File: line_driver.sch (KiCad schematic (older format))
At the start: 30 parts, among them J7 DRV632

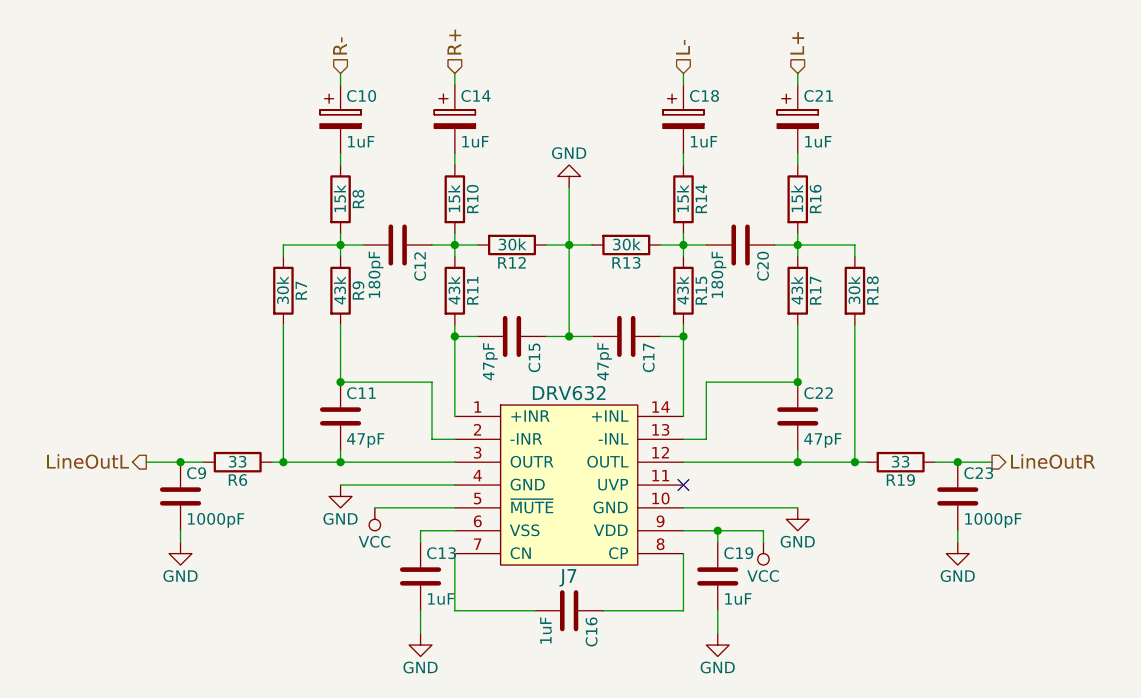
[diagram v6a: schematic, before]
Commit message: Voltage regulator adjustments and tidying
Switch to LD1117 component and add decoupling caps.
Add a decoupling cap to the audio switch
Shift some status LEDs to modules layer
Use ProMini instead of ProMicro
Update BOM
Update netlist
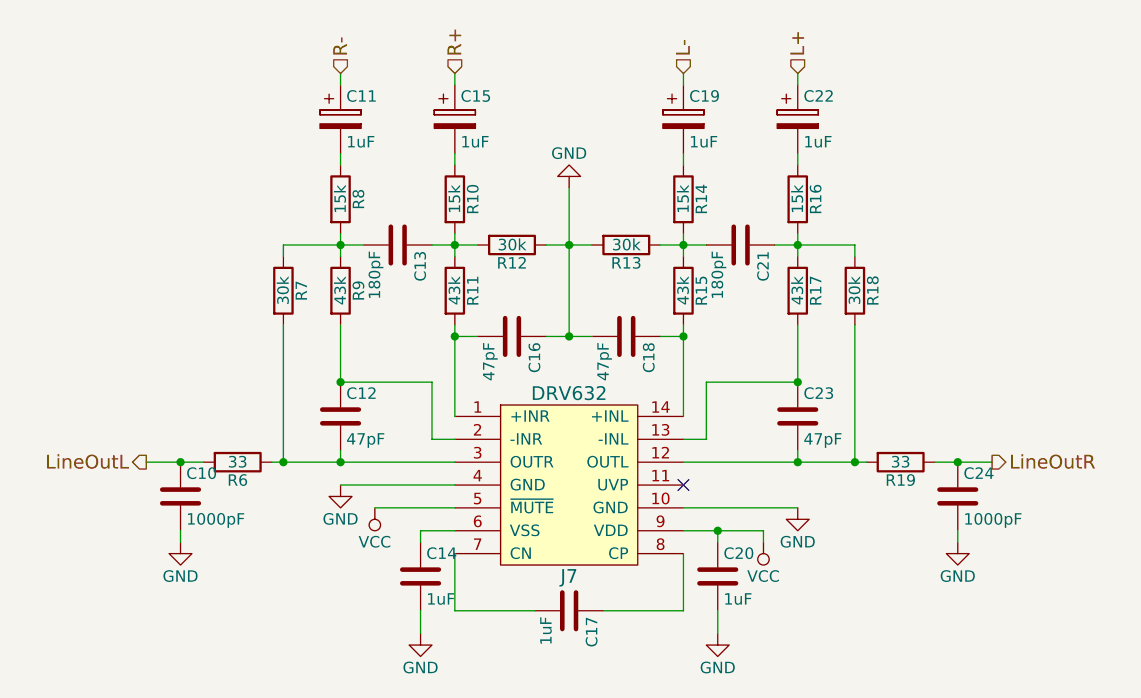
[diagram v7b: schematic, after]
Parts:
- C10: renamed from C9; footprint (none) -> blubaru:C_Disc_D5.5mm_W2.5mm_P2.50mm
- C11: renamed from C10; footprint (none) -> Capacitors_THT:CP_Radial_D4.0mm_P1.50mm
- C12: renamed from C11; footprint (none) -> blubaru:C_Disc_D5.5mm_W2.5mm_P2.50mm
- C13: renamed from C12; footprint (none) -> blubaru:C_Disc_D5.5mm_W2.5mm_P2.50mm
- C14: renamed from C13; footprint (none) -> blubaru:C_Disc_D5.5mm_W2.5mm_P2.50mm
- C15: renamed from C14; footprint (none) -> Capacitors_THT:CP_Radial_D4.0mm_P1.50mm
- C16: renamed from C15; footprint (none) -> blubaru:C_Disc_D5.5mm_W2.5mm_P2.50mm
- C17: renamed from C16; footprint (none) -> blubaru:C_Disc_D5.5mm_W2.5mm_P2.50mm
- C18: renamed from C17; footprint (none) -> blubaru:C_Disc_D5.5mm_W2.5mm_P2.50mm
- C19: renamed from C18; footprint (none) -> Capacitors_THT:CP_Radial_D4.0mm_P1.50mm
- C20: renamed from C19; footprint (none) -> blubaru:C_Disc_D5.5mm_W2.5mm_P2.50mm
- C21: renamed from C20; footprint (none) -> blubaru:C_Disc_D5.5mm_W2.5mm_P2.50mm
- C22: renamed from C21; footprint (none) -> Capacitors_THT:CP_Radial_D4.0mm_P1.50mm
- C23: renamed from C22; footprint (none) -> blubaru:C_Disc_D5.5mm_W2.5mm_P2.50mm
- C24: renamed from C23; footprint (none) -> blubaru:C_Disc_D5.5mm_W2.5mm_P2.50mm
- R19, R6: footprint (none) -> Resistors_THT:R_Axial_DIN0204_L3.6mm_D1.6mm_P1.90mm_Vertical
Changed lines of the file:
@@
 $EndComp
 $Comp
-L C C16
+L C C17
 U 1 1 59178EA2
 P 5800 3950
-F 0 "C16" H 5825 4050 50  0000 L CNN
+F 0 "C17" H 5825 4050 50  0000 L CNN
 F 1 "1uF" H 5825 3850 50  0000 L CNN
-F 2 "" H 5838 3800 50  0001 C CNN
+F 2 "blubaru:C_Disc_D5.5mm_W2.5mm_P2.50mm" H 5838 3800 50  0001 C CNN
 F 3 "" H 5800 3950 50  0001 C CNN
 	1    5800 3950
@@
 	6300 3500 6800 3500
 $Comp
-L C C13
+L C C14
 U 1 1 59178EFD
 P 5150 3800
-F 0 "C13" H 5175 3900 50  0000 L CNN
+F 0 "C14" H 5175 3900 50  0000 L CNN
 F 1 "1uF" H 5175 3700 50  0000 L CNN
-F 2 "" H 5188 3650 50  0001 C CNN
+F 2 "blubaru:C_Disc_D5.5mm_W2.5mm_P2.50mm" H 5188 3650 50  0001 C CNN
 F 3 "" H 5150 3800 50  0001 C CNN
 	1    5150 3800
@@
 	5150 3950 5150 4050
 $Comp
-L C C19
+L C C20
 U 1 1 59178FC9
 P 6450 3800
-F 0 "C19" H 6475 3900 50  0000 L CNN
+F 0 "C20" H 6475 3900 50  0000 L CNN
 F 1 "1uF" H 6475 3700 50  0000 L CNN
-F 2 "" H 6488 3650 50  0001 C CNN
+F 2 "blubaru:C_Disc_D5.5mm_W2.5mm_P2.50mm" H 6488 3650 50  0001 C CNN
 F 3 "" H 6450 3800 50  0001 C CNN
 	1    6450 3800
@@
 LineOutL
 $Comp
-L C C22
+L C C23
 U 1 1 59179109
 P 6800 3100
-F 0 "C22" H 6825 3200 50  0000 L CNN
+F 0 "C23" H 6825 3200 50  0000 L CNN
 F 1 "47pF" H 6825 3000 50  0000 L CNN
-F 2 "" H 6838 2950 50  0001 C CNN
+F 2 "blubaru:C_Disc_D5.5mm_W2.5mm_P2.50mm" H 6838 2950 50  0001 C CNN
 F 3 "" H 6800 3100 50  0001 C CNN
 	1    6800 3100
@@
 $EndComp
 $Comp
-L C C11
+L C C12
 U 1 1 5917915A
 P 4800 3100
-F 0 "C11" H 4825 3200 50  0000 L CNN
+F 0 "C12" H 4825 3200 50  0000 L CNN
 F 1 "47pF" H 4825 3000 50  0000 L CNN
-F 2 "" H 4838 2950 50  0001 C CNN
+F 2 "blubaru:C_Disc_D5.5mm_W2.5mm_P2.50mm" H 4838 2950 50  0001 C CNN
 F 3 "" H 4800 3100 50  0001 C CNN
 	1    4800 3100
@@
 	6400 3200 6300 3200
 $Comp
-L C C17
+L C C18
 U 1 1 591791B6
 P 6050 2750
-F 0 "C17" H 6075 2850 50  0000 L CNN
+F 0 "C18" H 6075 2850 50  0000 L CNN
 F 1 "47pF" H 6075 2650 50  0000 L CNN
-F 2 "" H 6088 2600 50  0001 C CNN
+F 2 "blubaru:C_Disc_D5.5mm_W2.5mm_P2.50mm" H 6088 2600 50  0001 C CNN
 F 3 "" H 6050 2750 50  0001 C CNN
 	1    6050 2750
@@
 $EndComp
 $Comp
-L C C15
+L C C16
 U 1 1 591791EB
 P 5550 2750
-F 0 "C15" H 5575 2850 50  0000 L CNN
+F 0 "C16" H 5575 2850 50  0000 L CNN
 F 1 "47pF" H 5575 2650 50  0000 L CNN
-F 2 "" H 5588 2600 50  0001 C CNN
+F 2 "blubaru:C_Disc_D5.5mm_W2.5mm_P2.50mm" H 5588 2600 50  0001 C CNN
 F 3 "" H 5550 2750 50  0001 C CNN
 	1    5550 2750
@@
 	5300 1950 5300 2000
 $Comp
-L C C12
+L C C13
 U 1 1 5917A56B
 P 5050 2350
-F 0 "C12" H 5075 2450 50  0000 L CNN
+F 0 "C13" H 5075 2450 50  0000 L CNN
 F 1 "180pF" H 5075 2250 50  0000 L CNN
-F 2 "" H 5088 2200 50  0001 C CNN
+F 2 "blubaru:C_Disc_D5.5mm_W2.5mm_P2.50mm" H 5088 2200 50  0001 C CNN
 F 3 "" H 5050 2350 50  0001 C CNN
 	1    5050 2350
@@
 $EndComp
 $Comp
-L C C20
+L C C21
 U 1 1 5917A5AC
 P 6550 2350
-F 0 "C20" H 6575 2450 50  0000 L CNN
+F 0 "C21" H 6575 2450 50  0000 L CNN
 F 1 "180pF" H 6575 2250 50  0000 L CNN
-F 2 "" H 6588 2200 50  0001 C CNN
+F 2 "blubaru:C_Disc_D5.5mm_W2.5mm_P2.50mm" H 6588 2200 50  0001 C CNN
 F 3 "" H 6550 2350 50  0001 C CNN
 	1    6550 2350
@@
 $EndComp
 $Comp
-L C C23
+L C C24
 U 1 1 5933924A
 P 7500 3450
-F 0 "C23" H 7525 3550 50  0000 L CNN
+F 0 "C24" H 7525 3550 50  0000 L CNN
 F 1 "1000pF" H 7525 3350 50  0000 L CNN
-F 2 "" H 7538 3300 50  0001 C CNN
+F 2 "blubaru:C_Disc_D5.5mm_W2.5mm_P2.50mm" H 7538 3300 50  0001 C CNN
 F 3 "" H 7500 3450 50  0001 C CNN
 	1    7500 3450
@@
 $EndComp
 $Comp
-L C C9
+L C C10
 U 1 1 593392DF
 P 4100 3450
-F 0 "C9" H 4125 3550 50  0000 L CNN
+F 0 "C10" H 4125 3550 50  0000 L CNN
 F 1 "1000pF" H 4125 3350 50  0000 L CNN
-F 2 "" H 4138 3300 50  0001 C CNN
+F 2 "blubaru:C_Disc_D5.5mm_W2.5mm_P2.50mm" H 4138 3300 50  0001 C CNN
 F 3 "" H 4100 3450 50  0001 C CNN
 	1    4100 3450
@@
 F 0 "R19" V 7330 3300 50  0000 C CNN
 F 1 "33" V 7250 3300 50  0000 C CNN
-F 2 "" V 7180 3300 50  0001 C CNN
+F 2 "Resistors_THT:R_Axial_DIN0204_L3.6mm_D1.6mm_P1.90mm_Vertical" V 7180 3300 50  0001 C CNN
 F 3 "" H 7250 3300 50  0001 C CNN
 	1    7250 3300
@@
 F 0 "R6" V 4430 3300 50  0000 C CNN
 F 1 "33" V 4350 3300 50  0000 C CNN
-F 2 "" V 4280 3300 50  0001 C CNN
+F 2 "Resistors_THT:R_Axial_DIN0204_L3.6mm_D1.6mm_P1.90mm_Vertical" V 4280 3300 50  0001 C CNN
 F 3 "" H 4350 3300 50  0001 C CNN
 	1    4350 3300
@@
 	4100 3600 4100 3650
 $Comp
-L CP C10
+L CP C11
 U 1 1 5939D955
 P 4800 1800
-F 0 "C10" H 4825 1900 50  0000 L CNN
+F 0 "C11" H 4825 1900 50  0000 L CNN
 F 1 "1uF" H 4825 1700 50  0000 L CNN
-F 2 "" H 4838 1650 50  0001 C CNN
+F 2 "Capacitors_THT:CP_Radial_D4.0mm_P1.50mm" H 4838 1650 50  0001 C CNN
 F 3 "" H 4800 1800 50  0001 C CNN
 	1    4800 1800
@@
 $EndComp
 $Comp
-L CP C14
+L CP C15
 U 1 1 5939DA1E
 P 5300 1800
-F 0 "C14" H 5325 1900 50  0000 L CNN
+F 0 "C15" H 5325 1900 50  0000 L CNN
 F 1 "1uF" H 5325 1700 50  0000 L CNN
-F 2 "" H 5338 1650 50  0001 C CNN
+F 2 "Capacitors_THT:CP_Radial_D4.0mm_P1.50mm" H 5338 1650 50  0001 C CNN
 F 3 "" H 5300 1800 50  0001 C CNN
 	1    5300 1800
@@
 $EndComp
 $Comp
-L CP C18
+L CP C19
 U 1 1 5939DA7F
 P 6300 1800
-F 0 "C18" H 6325 1900 50  0000 L CNN
+F 0 "C19" H 6325 1900 50  0000 L CNN
 F 1 "1uF" H 6325 1700 50  0000 L CNN
-F 2 "" H 6338 1650 50  0001 C CNN
+F 2 "Capacitors_THT:CP_Radial_D4.0mm_P1.50mm" H 6338 1650 50  0001 C CNN
 F 3 "" H 6300 1800 50  0001 C CNN
 	1    6300 1800
@@
 $EndComp
 $Comp
-L CP C21
+L CP C22
 U 1 1 5939DADA
 P 6800 1800
-F 0 "C21" H 6825 1900 50  0000 L CNN
+F 0 "C22" H 6825 1900 50  0000 L CNN
 F 1 "1uF" H 6825 1700 50  0000 L CNN
-F 2 "" H 6838 1650 50  0001 C CNN
+F 2 "Capacitors_THT:CP_Radial_D4.0mm_P1.50mm" H 6838 1650 50  0001 C CNN
 F 3 "" H 6800 1800 50  0001 C CNN
 	1    6800 1800

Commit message: Add new capacitor footprints and associate them.
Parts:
- C10, C12, C13, C16, C18, C21, C23, C24: footprint blubaru:C_Disc_D5.5mm_W2.5mm_P2.50mm -> blubaru:C_Disc_D4.0mm_W2.6mm_P2.50mm
- C14, C17, C20: footprint blubaru:C_Disc_D5.5mm_W2.5mm_P2.50mm -> blubaru:C_Disc_D5.0mm_W3.2mm_P2.50mm
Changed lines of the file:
@@
 F 0 "C17" H 5825 4050 50  0000 L CNN
 F 1 "1uF" H 5825 3850 50  0000 L CNN
-F 2 "blubaru:C_Disc_D5.5mm_W2.5mm_P2.50mm" H 5838 3800 50  0001 C CNN
+F 2 "blubaru:C_Disc_D5.0mm_W3.2mm_P2.50mm" H 5838 3800 50  0001 C CNN
 F 3 "" H 5800 3950 50  0001 C CNN
 	1    5800 3950
@@
 F 0 "C14" H 5175 3900 50  0000 L CNN
 F 1 "1uF" H 5175 3700 50  0000 L CNN
-F 2 "blubaru:C_Disc_D5.5mm_W2.5mm_P2.50mm" H 5188 3650 50  0001 C CNN
+F 2 "blubaru:C_Disc_D5.0mm_W3.2mm_P2.50mm" H 5188 3650 50  0001 C CNN
 F 3 "" H 5150 3800 50  0001 C CNN
 	1    5150 3800
@@
 F 0 "C20" H 6475 3900 50  0000 L CNN
 F 1 "1uF" H 6475 3700 50  0000 L CNN
-F 2 "blubaru:C_Disc_D5.5mm_W2.5mm_P2.50mm" H 6488 3650 50  0001 C CNN
+F 2 "blubaru:C_Disc_D5.0mm_W3.2mm_P2.50mm" H 6488 3650 50  0001 C CNN
 F 3 "" H 6450 3800 50  0001 C CNN
 	1    6450 3800
@@
 F 0 "C23" H 6825 3200 50  0000 L CNN
 F 1 "47pF" H 6825 3000 50  0000 L CNN
-F 2 "blubaru:C_Disc_D5.5mm_W2.5mm_P2.50mm" H 6838 2950 50  0001 C CNN
+F 2 "blubaru:C_Disc_D4.0mm_W2.6mm_P2.50mm" H 6838 2950 50  0001 C CNN
 F 3 "" H 6800 3100 50  0001 C CNN
 	1    6800 3100
@@
 F 0 "C12" H 4825 3200 50  0000 L CNN
 F 1 "47pF" H 4825 3000 50  0000 L CNN
-F 2 "blubaru:C_Disc_D5.5mm_W2.5mm_P2.50mm" H 4838 2950 50  0001 C CNN
+F 2 "blubaru:C_Disc_D4.0mm_W2.6mm_P2.50mm" H 4838 2950 50  0001 C CNN
 F 3 "" H 4800 3100 50  0001 C CNN
 	1    4800 3100
@@
 F 0 "C18" H 6075 2850 50  0000 L CNN
 F 1 "47pF" H 6075 2650 50  0000 L CNN
-F 2 "blubaru:C_Disc_D5.5mm_W2.5mm_P2.50mm" H 6088 2600 50  0001 C CNN
+F 2 "blubaru:C_Disc_D4.0mm_W2.6mm_P2.50mm" H 6088 2600 50  0001 C CNN
 F 3 "" H 6050 2750 50  0001 C CNN
 	1    6050 2750
@@
 F 0 "C16" H 5575 2850 50  0000 L CNN
 F 1 "47pF" H 5575 2650 50  0000 L CNN
-F 2 "blubaru:C_Disc_D5.5mm_W2.5mm_P2.50mm" H 5588 2600 50  0001 C CNN
+F 2 "blubaru:C_Disc_D4.0mm_W2.6mm_P2.50mm" H 5588 2600 50  0001 C CNN
 F 3 "" H 5550 2750 50  0001 C CNN
 	1    5550 2750
@@
 F 0 "C13" H 5075 2450 50  0000 L CNN
 F 1 "180pF" H 5075 2250 50  0000 L CNN
-F 2 "blubaru:C_Disc_D5.5mm_W2.5mm_P2.50mm" H 5088 2200 50  0001 C CNN
+F 2 "blubaru:C_Disc_D4.0mm_W2.6mm_P2.50mm" H 5088 2200 50  0001 C CNN
 F 3 "" H 5050 2350 50  0001 C CNN
 	1    5050 2350
@@
 F 0 "C21" H 6575 2450 50  0000 L CNN
 F 1 "180pF" H 6575 2250 50  0000 L CNN
-F 2 "blubaru:C_Disc_D5.5mm_W2.5mm_P2.50mm" H 6588 2200 50  0001 C CNN
+F 2 "blubaru:C_Disc_D4.0mm_W2.6mm_P2.50mm" H 6588 2200 50  0001 C CNN
 F 3 "" H 6550 2350 50  0001 C CNN
 	1    6550 2350
@@
 F 0 "C24" H 7525 3550 50  0000 L CNN
 F 1 "1000pF" H 7525 3350 50  0000 L CNN
-F 2 "blubaru:C_Disc_D5.5mm_W2.5mm_P2.50mm" H 7538 3300 50  0001 C CNN
+F 2 "blubaru:C_Disc_D4.0mm_W2.6mm_P2.50mm" H 7538 3300 50  0001 C CNN
 F 3 "" H 7500 3450 50  0001 C CNN
 	1    7500 3450
@@
 F 0 "C10" H 4125 3550 50  0000 L CNN
 F 1 "1000pF" H 4125 3350 50  0000 L CNN
-F 2 "blubaru:C_Disc_D5.5mm_W2.5mm_P2.50mm" H 4138 3300 50  0001 C CNN
+F 2 "blubaru:C_Disc_D4.0mm_W2.6mm_P2.50mm" H 4138 3300 50  0001 C CNN
 F 3 "" H 4100 3450 50  0001 C CNN
 	1    4100 3450
